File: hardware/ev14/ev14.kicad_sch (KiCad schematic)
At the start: 165 parts, among them CN1 Conn_05x02_Female, CN2 PJ-242, J1 USB_C_Receptacle, J10 Conn_02x04_Odd_Even, J11 Conn_02x05_Counter_Clockwise, J2 Conn_01x02_Socket, J3 AudioJack4, J5 Conn_02x03_Odd_Even, J6 Conn_01x35_Socket, J7 Conn_02x05_Counter_Clockwise, J8 Conn_02x05_Counter_Clockwise, J9 Conn_02x05_Counter_Clockwise, Q1 2N7002, SW1 SW_SPDT, SW2 SW_Push, SW3 SW_Push, SW4 SW_Push, SW5 SW_Push, U1 BQ21040DBV, U10 STM32F405RGTx, U2 USBLC6-2P6, U3 STM32F072CBTx, U4 CH340C, U5 TPS63060, U6 WM8960CGEFL/RV, U7 ESP32-S3-WROOM-1, U8 M24C02-RMN6TP, U9 BM14B(0.8)-24DS-0.4V(53), Y1 Crystal_GND24

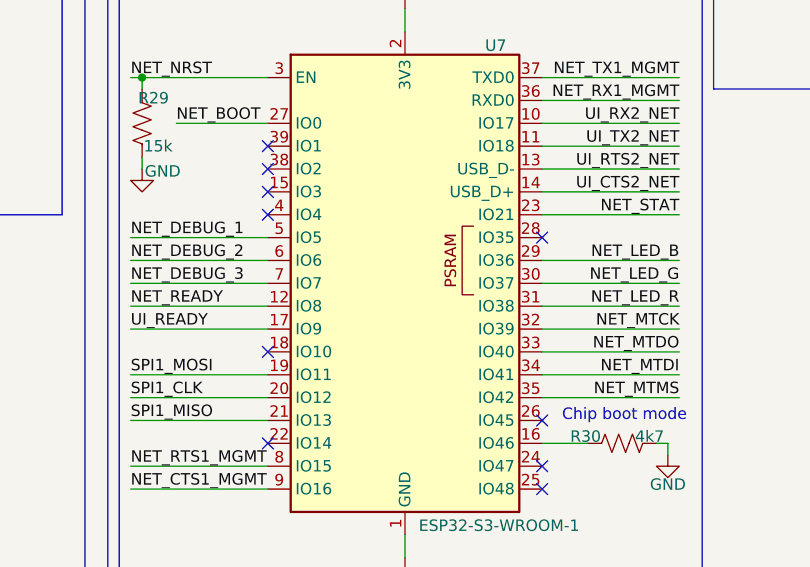
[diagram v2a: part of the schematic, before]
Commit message: chore: replaced boot/reset buttons with one in stock, added rotation and position offsets
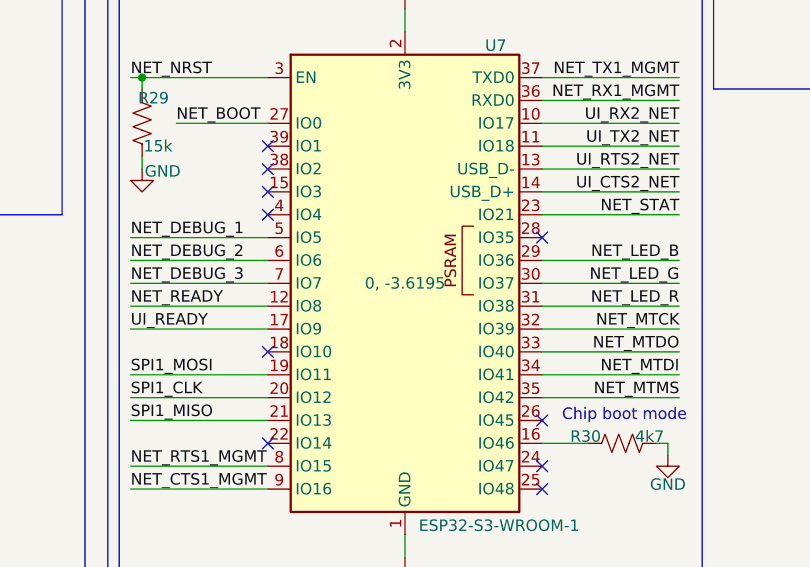
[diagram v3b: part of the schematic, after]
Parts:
- CN2: FT Rotation Offset (none) -> 90
- J1: FT Position Offset 0,1.397 -> (none)
- J3: FT Rotation Offset (none) -> -90
- SW1: FT Position Offset 0,-3.556 -> (none)
- SW2, SW3: footprint Hactar_Footprints:SW-SMD_YIYUAN_YTS1C003XXX -> Hactar_Footprints:SW-SMD_SHOU_TS36CA-0.6; JLCPCB Part # C5188566 -> C2906288
- U7: FT Position Offset (none) -> 0, -3.6195
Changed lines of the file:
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@@
 			)
 		)
-		(property "Sim.Device" ""
+		(property "FT Position Offset" "0, -3.6195"
 			(at 245.11 113.03 0)
 			(effects
@@
 			)
 		)
+		(property "FT Rotation Offset" "-90"
+			(at 328.93 231.14 0)
+			(effects
+				(font
+					(size 1.27 1.27)
+				)
+				(hide yes)
+			)
+		)
 		(pin "S"
 		)
@@
 			)
 		)
-		(property "Footprint" "Hactar_Footprints:SW-SMD_YIYUAN_YTS1C003XXX"
+		(property "Footprint" "Hactar_Footprints:SW-SMD_SHOU_TS36CA-0.6"
 			(at 167.64 115.57 0)
 			(effects
@@
 			)
 		)
-		(property "JLCPCB Part #" "C5188566"
+		(property "JLCPCB Part #" "C2906288"
 			(at 167.64 120.65 0)
 			(effects
@@
 			)
 		)
-		(property "FT Position Offset" "0,1.397"
-			(at 41.91 234.95 0)
-			(effects
-				(font
-					(size 1.27 1.27)
-				)
-				(hide yes)
-			)
-		)
-		(property "Availability" ""
-			(at 41.91 234.95 0)
-			(effects
-				(font
-					(size 1.27 1.27)
-				)
-			)
-		)
-		(property "Sim.Device" ""
-			(at 41.91 234.95 0)
-			(effects
-				(font
-					(size 1.27 1.27)
-				)
-			)
-		)
 		(pin "A1"
 		)
@@
 			)
 		)
-		(property "FT Position Offset" "0,-3.556"
-			(at 104.14 306.07 0)
-			(effects
-				(font
-					(size 1.27 1.27)
-				)
-				(hide yes)
-			)
-		)
-		(property "Availability" ""
-			(at 104.14 306.07 0)
-			(effects
-				(font
-					(size 1.27 1.27)
-				)
-			)
-		)
-		(property "Sim.Device" ""
-			(at 104.14 306.07 0)
-			(effects
-				(font
-					(size 1.27 1.27)
-				)
-			)
-		)
 		(pin "2"
 		)
@@
 			)
 		)
-		(property "Footprint" "Hactar_Footprints:SW-SMD_YIYUAN_YTS1C003XXX"
+		(property "Footprint" "Hactar_Footprints:SW-SMD_SHOU_TS36CA-0.6"
 			(at 157.48 148.59 0)
 			(effects
@@
 			)
 		)
-		(property "JLCPCB Part #" "C5188566"
+		(property "JLCPCB Part #" "C2906288"
 			(at 157.48 153.67 0)
 			(effects
@@
 			(at 328.93 213.36 0)
 			(effects
+				(font
+					(size 1.27 1.27)
+				)
+				(hide yes)
+			)
+		)
+		(property "FT Rotation Offset" "90"
+			(at 328.93 213.36 0)
+			(effects
